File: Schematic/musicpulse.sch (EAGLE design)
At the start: 19 parts, among them IC1 UA78M33DCY

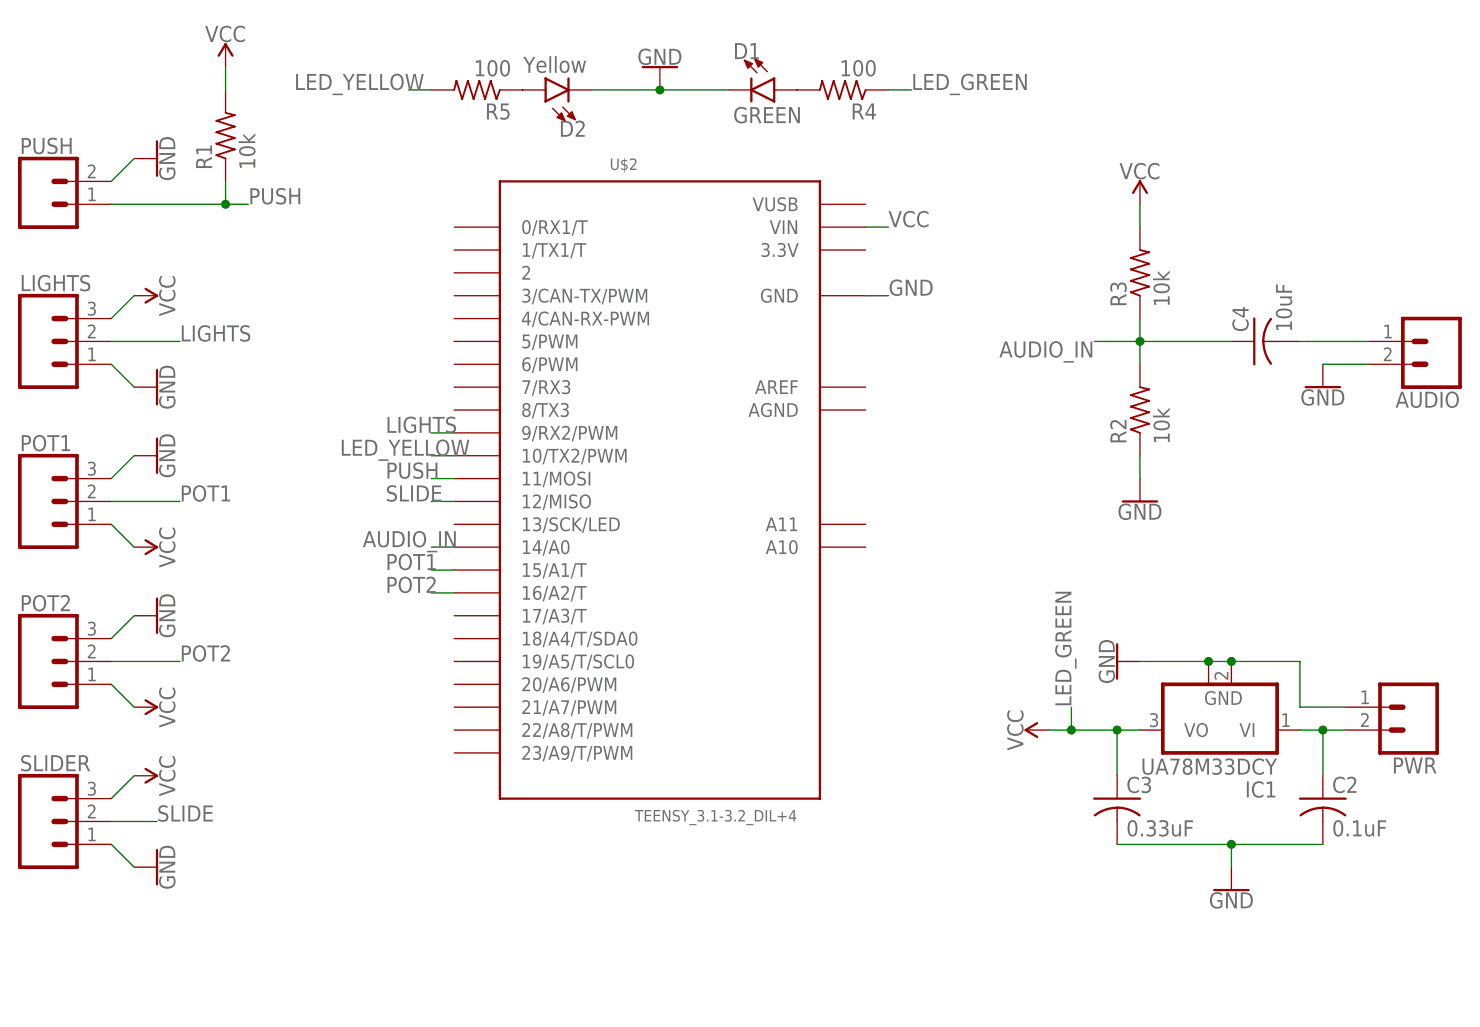
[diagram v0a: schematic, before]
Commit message: Changed to through hole. Adjusted some resistor files. Rerouted board. Reprocessed gerbers. Added board and schematic reference pictures.
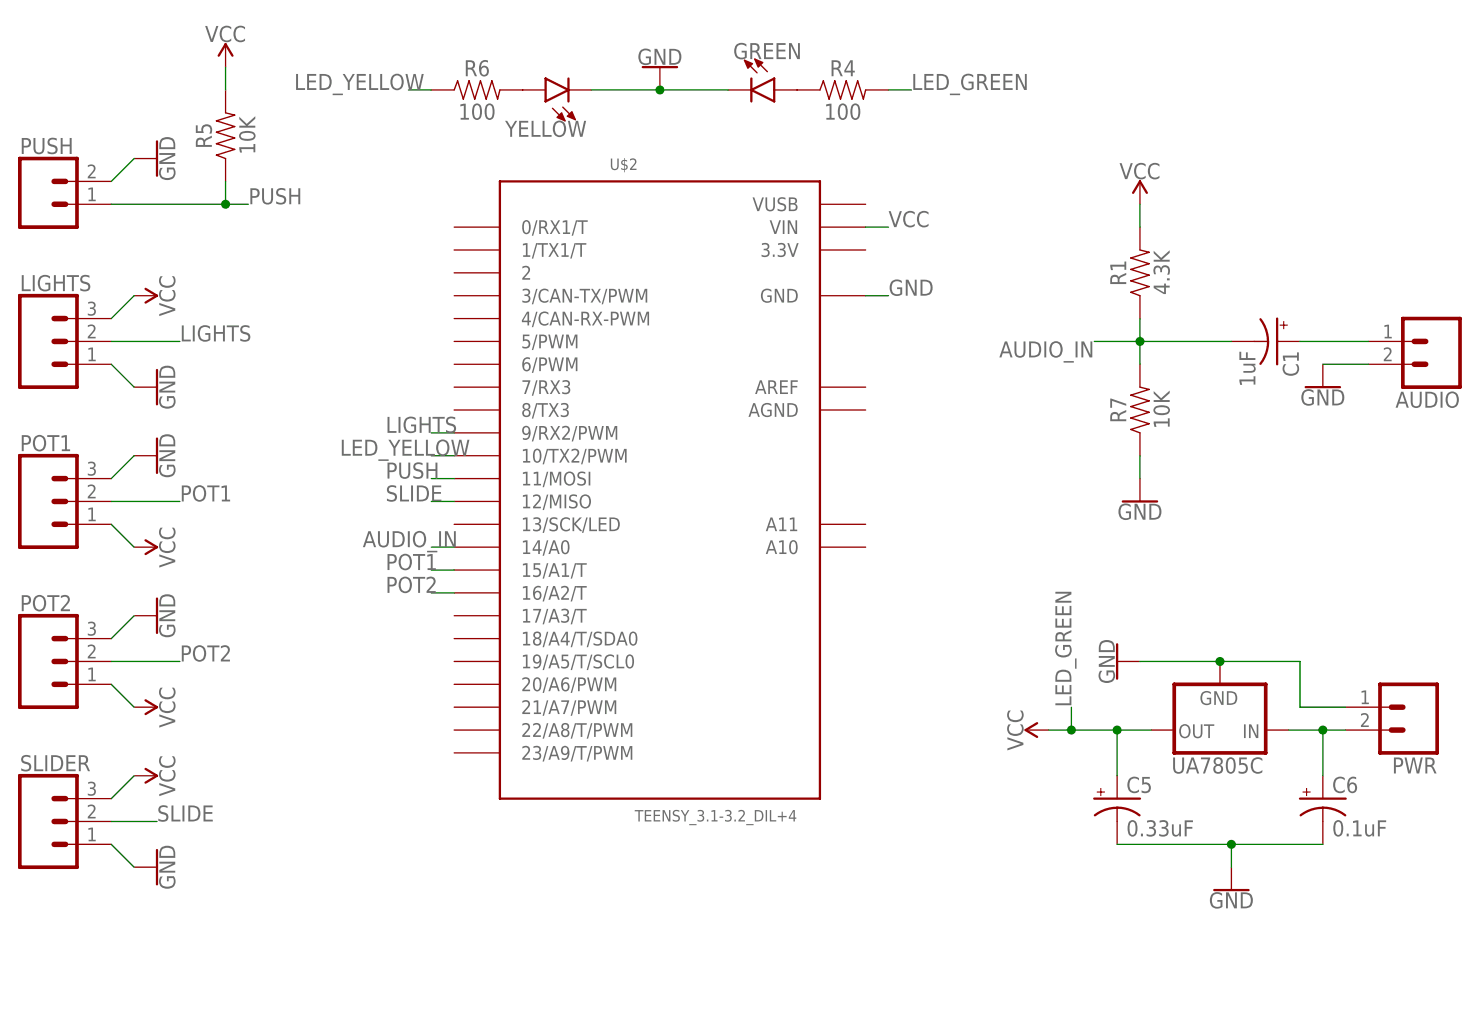
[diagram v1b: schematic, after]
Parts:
- removed C2: 0.1uF, BeagleBone_Black_Wireless:C-USC1206
- removed C3: 0.33uF, BeagleBone_Black_Wireless:C-USC1206
- removed C4: 10uF, BeagleBone_Black_Wireless:C-USC1206
- removed D1: GREEN, SparkFun-LED:LED-GREEN1206
- removed D2: Yellow, SparkFun-LED:LED-YELLOWLILYPAD
- removed IC1: UA78M33DCY, linear:UA78M33DCY
- removed R2, R3: 10k, BeagleBone_Black_Wireless:R-US_R1206
- added C1: 1uF, SparkFun-Capacitors:10UF-POLAR-RADIAL-2.5MM-25V-20%
- added C5: 0.33uF, SparkFun-Capacitors:10UF-POLAR-RADIAL-2.5MM-25V-20%
- added C6: 0.1uF, SparkFun-Capacitors:10UF-POLAR-RADIAL-2.5MM-25V-20%
- added GREEN, YELLOW: (no value), SparkFun-LED:LED-3MM-NO_SILK
- added R6: 100, SparkFun-Resistors:1KOHM-HORIZ-1/4W-1%
- added R7: 10K, SparkFun-Resistors:1KOHM-HORIZ-1/4W-1%
- added UA7805C: (no value), SparkFun-IC-Power:V_REG_78XXSINK
- R1: value 10k -> 4.3K; device BeagleBone_Black_Wireless:R-US_R1206 -> SparkFun-Resistors:1KOHM-HORIZ-1/4W-1%
- R4: device BeagleBone_Black_Wireless:R-US_R1206 -> SparkFun-Resistors:1KOHM-HORIZ-1/4W-1%
- R5: value 100 -> 10K; device BeagleBone_Black_Wireless:R-US_R1206 -> SparkFun-Resistors:1KOHM-HORIZ-1/4W-1%
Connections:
- net AUDIO_IN: now also C1.-, R1.1, R7.2; no longer C4.1, R2.2, R3.1
- net GND: now also C5.-, C6.-, GREEN.C, R7.1, UA7805C.GND, YELLOW.C; no longer C2.2, C3.2, D1.C, D2.C, IC1.GND, IC1.GND@1, R2.1
- net LED_GREEN: now also C5.+, R4.2, UA7805C.OUT; no longer C3.1, IC1.VO, R4.1
- net LED_YELLOW: now also R6.1; no longer R5.2
- net N$1: now also C6.+, UA7805C.IN; no longer C2.1, IC1.VI
- net N$2: now also R6.2, YELLOW.A; no longer D1.A, R4.2
- net N$3: now also R5.2; no longer R1.2
- net N$4: now also GREEN.A, R4.1; no longer D2.A, R5.1
- net N$5: now also C1.+; no longer C4.2
- net PUSH: now also R5.1; no longer R1.1
- net VCC: now also R1.2; no longer R3.2
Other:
- moved on the sheet: R1, R4, R5

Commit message: Rerouted board. Added pullup to slider. Changed some resistor values.
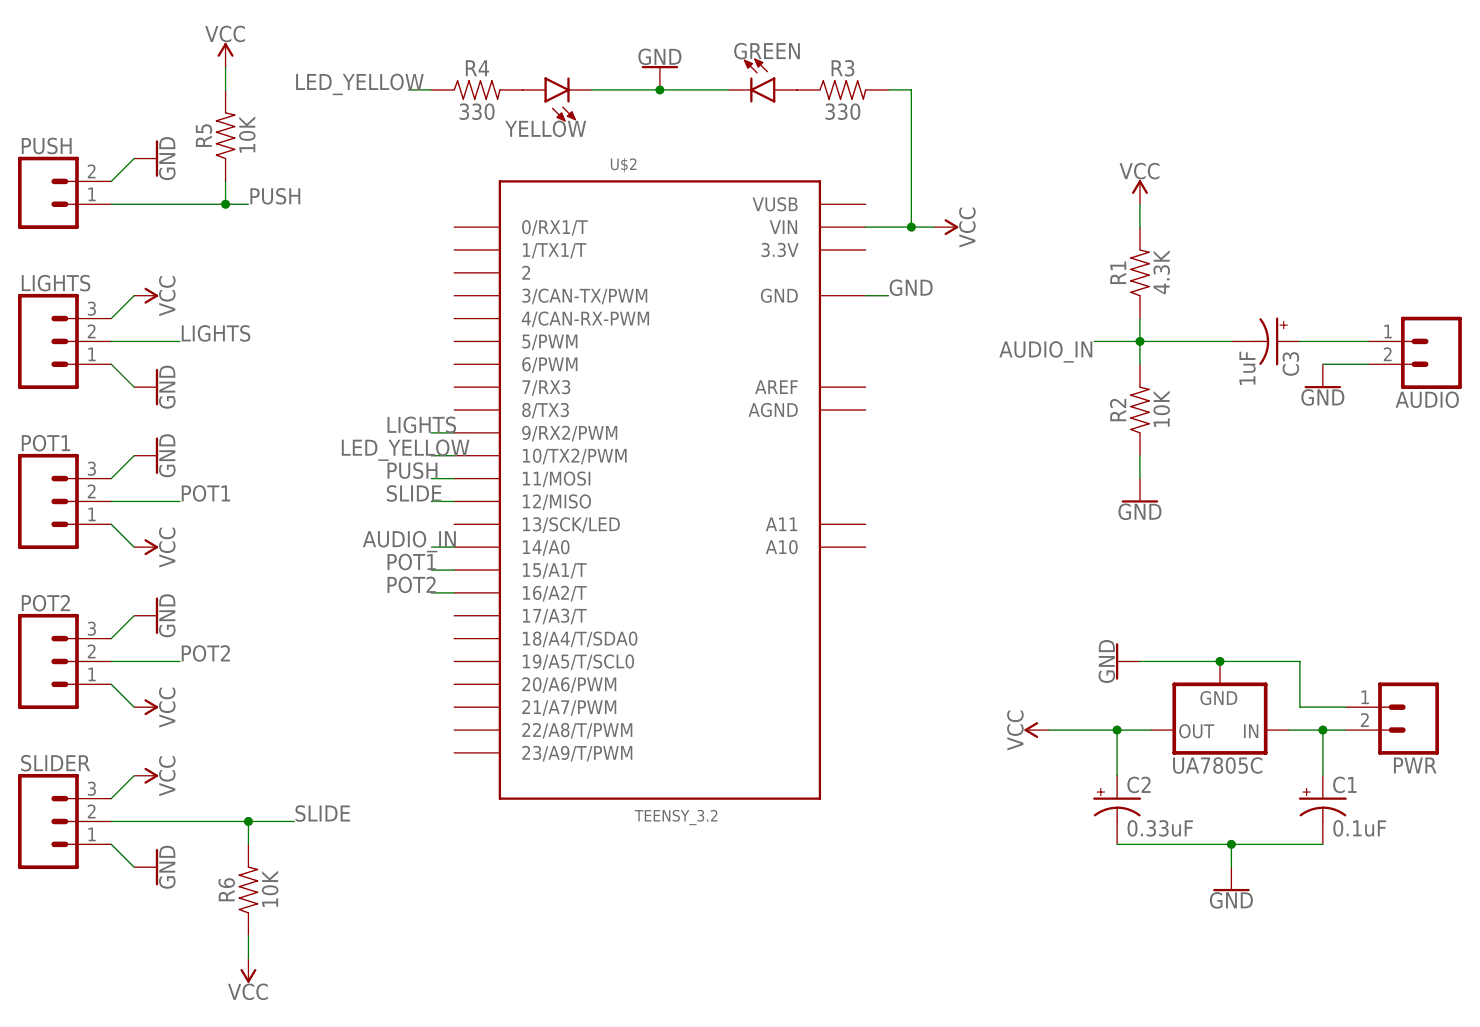
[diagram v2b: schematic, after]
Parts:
- removed C6: 0.1uF, SparkFun-Capacitors:10UF-POLAR-RADIAL-2.5MM-25V-20%
- added C3: 1uF, SparkFun-Capacitors:10UF-POLAR-RADIAL-2.5MM-25V-20%
- added R3: 330, SparkFun-Resistors:1KOHM-HORIZ-1/4W-1%
- C1: value 1uF -> 0.1uF
- R4: value 100 -> 330
- R6: value 100 -> 10K
- U$2: value TEENSY_3.1-3.2_DIL+4 -> TEENSY_3.2
- renumbered C5 to C2, R7 to R2
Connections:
- removed net LED_GREEN: C2.+, R4.2, UA7805C.OUT
- net AUDIO_IN: now also C3.-; no longer C1.-
- net GND: now also C1.-; no longer C6.-
- net LED_YELLOW: now also R4.1; no longer R6.1
- net N$1: now also C1.+; no longer C6.+
- net N$2: now also R4.2; no longer R6.2
- net N$4: now also R3.1; no longer R4.1
- net N$5: now also C3.+; no longer C1.+
- net SLIDE: now also R6.2
- net VCC: now also C2.+, R3.2, R6.1, UA7805C.OUT
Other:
- moved on the sheet: C1, R4, R6

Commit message: Added missing trace. Reprocessed CAM files.
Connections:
- removed net N$3: R5.2
- net VCC: now also R5.2
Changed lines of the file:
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@@
 <wire x1="35.56" y1="7.62" x2="35.56" y2="10.16" width="0.1524" layer="91"/>
+</segment>
+<segment>
+<pinref part="R5" gate="G$1" pin="2"/>
+<pinref part="SUPPLY6" gate="G$1" pin="VCC"/>
+<wire x1="33.02" y1="104.14" x2="33.02" y2="106.68" width="0.1524" layer="91"/>
 </segment>
 </net>
@@
 </segment>
 </net>
-<net name="N$3" class="0">
-<segment>
-<wire x1="33.02" y1="104.14" x2="33.02" y2="106.68" width="0.1524" layer="91"/>
-<pinref part="SUPPLY6" gate="G$1" pin="VCC"/>
-<pinref part="R5" gate="G$1" pin="2"/>
-</segment>
-</net>
